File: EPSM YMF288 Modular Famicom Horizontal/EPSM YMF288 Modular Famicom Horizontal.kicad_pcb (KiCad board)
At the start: 2 copper layers, 99 x 91.7 mm, 35 parts, among them J1 EPSM_DATA, J2 EPSM_AUDIO, J3 EPSM_SND_OUT, J4 EPSM_ADDR, J5 CONSOLE_M, J6 CARTRIDGE_F, U1 YMF288, U2 74HCT541, U3 74HCT541, U4 74HCT541, U5 74HCT541, X1 SG-8002CA

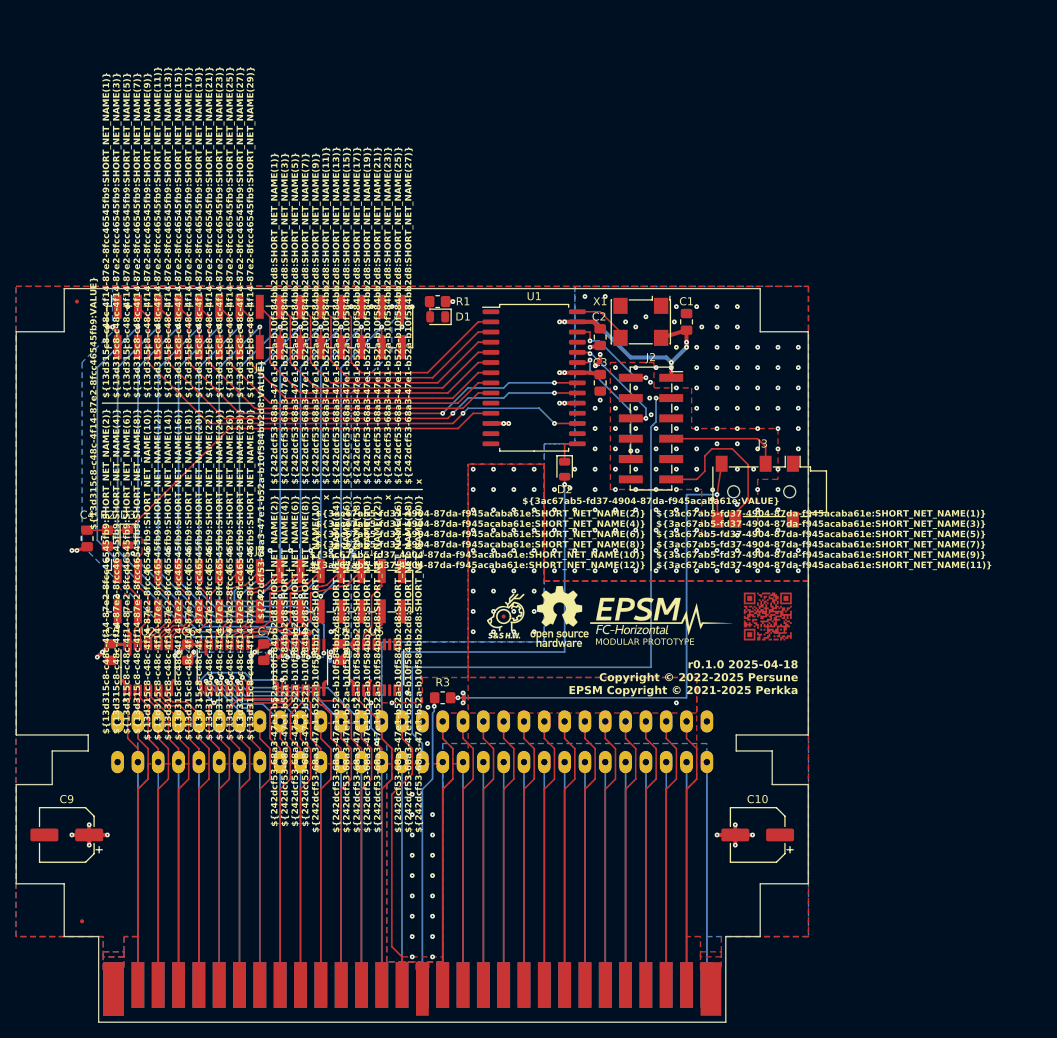
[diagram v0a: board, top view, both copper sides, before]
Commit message: fix: Fix YMF288 wiring and reset
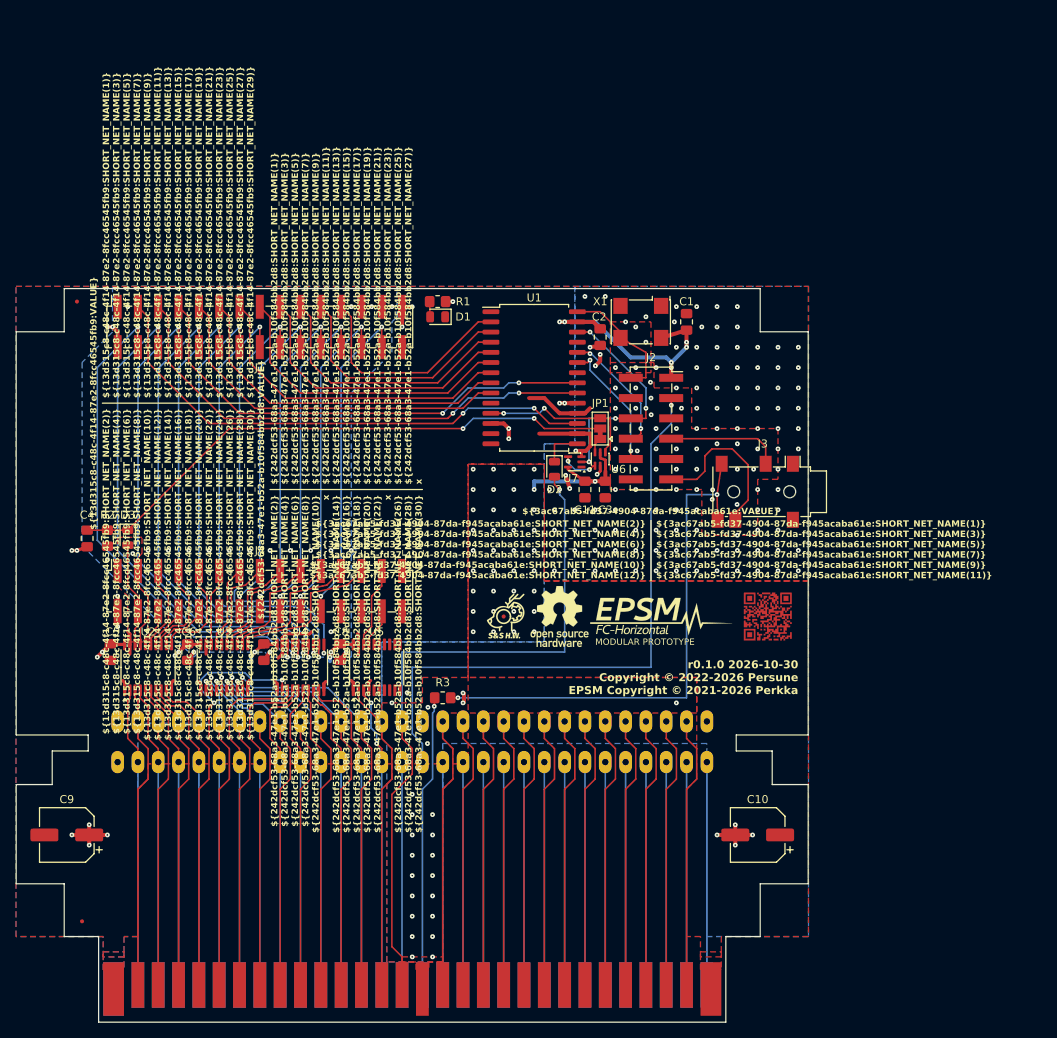
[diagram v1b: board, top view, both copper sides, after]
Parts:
- added C11: 0.1uF, Capacitor_SMD:C_0805_2012Metric_Pad1.18x1.45mm_HandSolder, F.Cu at (148.6, 71.1)
- added JP1: ~, Jumper:SolderJumper-3_P1.3mm_Bridged12_Pad1.0x1.5mm, F.Cu at (150.5, 63.5)
- added U6: 74LVC1G175, Package_TO_SOT_SMD:SOT-363_SC-70-6, F.Cu at (150.5, 67.3)
- added U7: 74LVC1GU04, Package_TO_SOT_SMD:SOT-353_SC-70-5, F.Cu at (147.3, 67.7)
- moved C3 13.4 mm to (151.1, 71.1)
- moved D2 1.27 mm to (144.8, 68.6)
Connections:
- C4 pad 1: /~{RESET} -> /~{M2_HALT}
- D3 pad 1: /~{RESET} -> /~{M2_HALT}
- J2 pad 2: /YM_LRCK -> /CLK_8MHz
- J2 pad 6: /YM_SDAT -> /YM_LRCK
- J2 pad 8: GND -> /YM_SDAT
- R2 pad 1: /~{RESET} -> /~{M2_HALT}
- U1 pad 22: VCC -> unconnected-(U1-~{STBY}-Pad22)
- U1 pad 28: Net-(U1-FMOSC) -> /CLK_8MHz
- X1 pad 3: Net-(U1-FMOSC) -> /CLK_8MHz
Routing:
- net /~{M2_HALT}: track 0.00 -> 70.4 mm, vias 0 -> 2
- net /~{RESET}: track 56.5 -> 20.2 mm, vias 0 -> 2
- net GND: track 39.9 -> 62.3 mm, vias 196 -> 192
- net /CLK_8MHz: track 0.00 -> 15.9 mm
- net /YM_LRCK: track 13.5 -> 28.8 mm, vias 2 -> 4
- net VCC: track 83.6 -> 97.5 mm, vias 69 -> 68
- net Net-(U1-FMOSC): track 7.18 -> 0.00 mm
- net Net-(U6-C): track 0.00 -> 4.67 mm, vias 0 -> 2
- net Net-(JP1-A): track 0.00 -> 1.94 mm
- net Net-(D2-K): track 3.83 -> 5.10 mm
- net /YM_SDAT: track 14.6 -> 15.9 mm
- net /AUD_RF: track 78.0 -> 77.0 mm
- net /~{IRQ}: track 86.0 -> 86.5 mm

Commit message: fix: Update processed rounded tracks
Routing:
- net /YM_LRCK: track 28.8 -> 29.7 mm
